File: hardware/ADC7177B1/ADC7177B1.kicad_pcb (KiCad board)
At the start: 4 copper layers, 160 x 100 mm, 185 parts, among them J1 20021111-00010T4LF, J2 RJ45_Wuerth_7499010121A, J3 1715721, J4 Conn_01x01, J5 Conn_01x01, J6 Conn_01x01, J7 Conn_01x01, K1 G6SK-2F-DC5, Q1 SI5618A, Q2 MMBT3904, Q3 FZT851, Q4 FZT951, Q5 FZT851, Q6 MMBT3904, Q7 MMBT3904, U1 STM32H743VITx, U10 TPS7A4901DGN, U11 ADC7177M1, U12 AD8599ARZ, U13 AD8599ARZ, U14 CPC1002N, U15 CPC1002N, U2 24LC08B-E/MS, U3 LAN8742A, U4 THN 15-2425, U5 TEC 3-2419WI, U6 TPS7A4901DGN, U7 TPS7A3001DGN, U8 TPS7A4901DGN, U9 TPS7A4901DGN, Y1 NX5032GA-16, Y2 NX5032GA-25

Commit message: PCB
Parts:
- added H5: MountingHole, MountingHole:MountingHole_2.5mm_Pad_TopBottom, F.Cu at (147.4, 91.4)
- added H6: MountingHole, MountingHole:MountingHole_2.5mm_Pad_TopBottom, F.Cu at (195.4, 91.4)
- added H7: MountingHole, MountingHole:MountingHole_2.5mm_Pad_TopBottom, F.Cu at (147.4, 114.4)
- added H8: MountingHole, MountingHole:MountingHole_2.5mm_Pad_TopBottom, F.Cu at (195.4, 114.4)
- R13, R14: moved to B.Cu
- moved R14 7.73 mm to (237.6, 111.8), turned to -90 degrees
- moved Q2 6.75 mm to (236.0, 105.7)
- moved D3 6.75 mm to (236.0, 108.8)
- moved C30 6.62 mm to (219.8, 96.2)
- moved C33 6.42 mm to (216.3, 96.3)
- moved R12 6.35 mm to (232.0, 100.6), turned to -90 degrees
- moved Q1 6.10 mm to (235.1, 100.7), turned to 90 degrees
- moved D2 5.05 mm to (232.0, 105.7), turned to 90 degrees
- moved R13 3.86 mm to (237.9, 102.9), turned to -90 degrees
- moved C16 3.50 mm to (205.9, 124.7), turned to 0 degrees
- moved C19 3.42 mm to (209.3, 124.7), turned to 180 degrees
- moved C31 1.89 mm to (208.4, 71.8), turned to -90 degrees
- moved C32 1.89 mm to (205.9, 74.9), turned to 90 degrees
- moved C11 1.66 mm to (194.9, 131.3), turned to -90 degrees
- moved C29 1.40 mm to (207.1, 86.9), turned to -90 degrees
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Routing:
- net +15V: track 5.00 -> 127.3 mm, vias 1 -> 6
- net -15V: track 5.08 -> 121.3 mm, vias 1 -> 6
- net +5VD: track 5.71 -> 94.6 mm, vias 2 -> 9
- net Net-(D4-A): track 0.00 -> 68.5 mm, vias 0 -> 9
- net +24V: track 0.00 -> 47.7 mm
- net Net-(D5-K): track 0.00 -> 40.6 mm, vias 0 -> 9
- net GND: track 2.12 -> 40.7 mm, vias 0 -> 42
- net VCCQ: track 0.00 -> 22.2 mm, vias 0 -> 2
- net /Schematic/Ethernet/LED2: track 0.00 -> 17.4 mm, vias 0 -> 1
- net +3.3V: track 15.7 -> 32.5 mm, vias 9 -> 16
- net Net-(D4-K): track 0.00 -> 13.9 mm
- net Net-(D5-A): track 0.00 -> 9.85 mm
- net /Schematic/Ethernet/LED1: track 0.00 -> 9.79 mm
- net Net-(D2-A): track 0.00 -> 9.74 mm
- net Net-(U3-XTAL2): track 0.00 -> 8.38 mm
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- added copper zone on F.Cu, net +15V
- added copper zone on B.Cu, net +24V
- added copper zone on In2.Cu, net +24V
- added copper zone on F.Cu, net +3.3V
- added copper zone on In2.Cu, net +3.3V
- added copper zone on F.Cu, net +5VA
- added copper zone on F.Cu, net +5VD
- added copper zone on In2.Cu, net +5VD
- added copper zone on F.Cu, net -15V
- added copper zone on B.Cu, net GND
- added copper zone on F.Cu, net GND
- added copper zone on In1.Cu, net GND
- added copper zone on B.Cu, net GNDS
- added copper zone on F.Cu, net GNDS
- added copper zone on In1.Cu, net GNDS
- added copper zone on F.Cu, net Net-(D4-A)
- added copper zone on In2.Cu, net Net-(D4-A)
- added copper zone on F.Cu, net Net-(D4-K)
- added copper zone on F.Cu, net Net-(D5-A)
- added copper zone on F.Cu, net Net-(D5-K)
- added copper zone on In2.Cu, net Net-(D5-K)
- added copper zone on F.Cu, net Net-(D6-A)
- added copper zone on In2.Cu, net Net-(D6-A)
- added copper zone on F.Cu, net Net-(D6-K)
- added copper zone on B.Cu, net Net-(J3-Pin_1)
- added copper zone on F.Cu, net Net-(Q3-B)
- added copper zone on F.Cu, net Net-(Q4-B)
- added copper zone on F.Cu, net Net-(Q5-B)
- added copper zone on F.Cu, net Net-(U4-+Vout)
- added copper zone on F.Cu, net Net-(U4--Vout)
- added copper zone on F.Cu, net Net-(U5-+Vout)

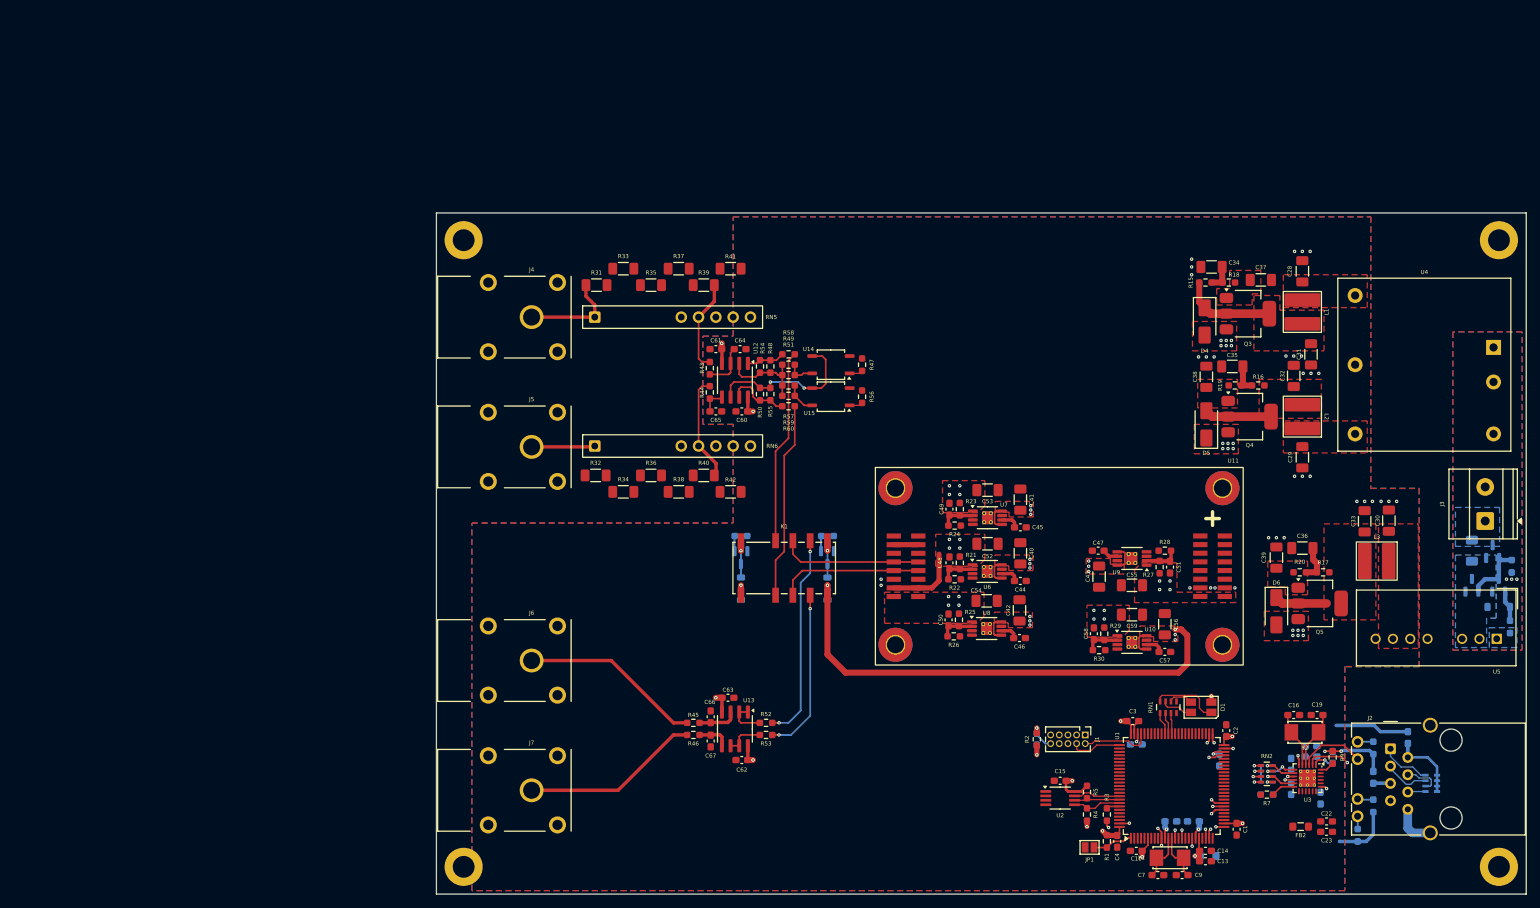
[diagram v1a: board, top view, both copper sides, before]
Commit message: Schematic changes
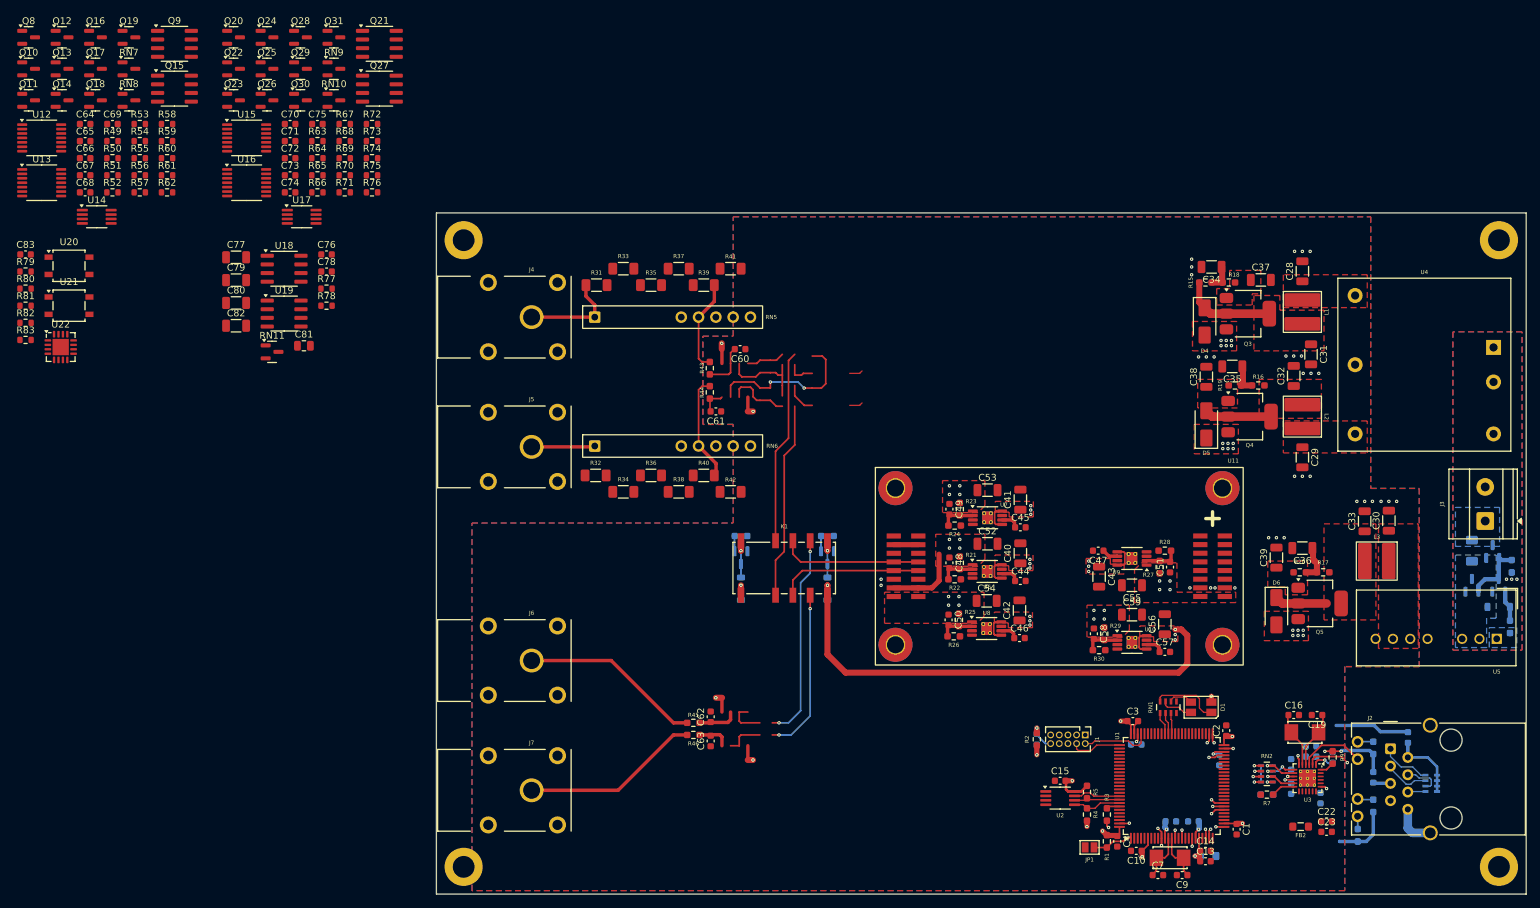
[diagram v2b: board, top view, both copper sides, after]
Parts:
- removed the C60 at (124.8, 80.1)
- removed the C61 at (121.0, 71.0)
- removed the C62 at (124.8, 131.3)
- removed the C63 at (122.8, 122.2)
- removed the R47 at (142.5, 73.3)
- removed the R48 at (129.0, 73.5)
- added C64: 0.1u, Capacitor_SMD:C_0603_1608Metric, F.Cu at (28.4, 37.9)
- added C65: 0.1u, Capacitor_SMD:C_0603_1608Metric, F.Cu at (28.4, 40.5)
- added C66: 0.1u, Capacitor_SMD:C_0603_1608Metric, F.Cu at (28.4, 43.0)
- added C67: 0.1u, Capacitor_SMD:C_0603_1608Metric, F.Cu at (28.4, 45.5)
- added C68: 0.1u, Capacitor_SMD:C_0603_1608Metric, F.Cu at (28.4, 48.0)
- added C69: 0.1u, Capacitor_SMD:C_0603_1608Metric, F.Cu at (32.4, 37.9)
- added C70: 0.1u, Capacitor_SMD:C_0603_1608Metric, F.Cu at (58.5, 37.9)
- added C71: 0.1u, Capacitor_SMD:C_0603_1608Metric, F.Cu at (58.5, 40.5)
- added C72: 0.1u, Capacitor_SMD:C_0603_1608Metric, F.Cu at (58.5, 43.0)
- added C73: 0.1u, Capacitor_SMD:C_0603_1608Metric, F.Cu at (58.5, 45.5)
- added C74: 0.1u, Capacitor_SMD:C_0603_1608Metric, F.Cu at (58.5, 48.0)
- added C75: 0.1u, Capacitor_SMD:C_0603_1608Metric, F.Cu at (62.5, 37.9)
- added C76: 0.1u, Capacitor_SMD:C_0603_1608Metric, F.Cu at (63.9, 57.1)
- added C77: 10u, Capacitor_SMD:C_1206_3216Metric, F.Cu at (50.6, 57.5)
- added C78: 0.1u, Capacitor_SMD:C_0603_1608Metric, F.Cu at (63.9, 59.6)
- added C79: 10u, Capacitor_SMD:C_1206_3216Metric, F.Cu at (50.6, 60.9)
- added C80: 10u, Capacitor_SMD:C_1206_3216Metric, F.Cu at (50.6, 64.2)
- added C81: 2u2, Capacitor_SMD:C_0805_2012Metric, F.Cu at (60.5, 70.5)
- added C82: 10u, Capacitor_SMD:C_1206_3216Metric, F.Cu at (50.6, 67.6)
- added C83: 100p, Capacitor_SMD:C_0603_1608Metric, F.Cu at (19.7, 57.1)
- added Q10: MMBT6429, Package_TO_SOT_SMD:SOT-23, F.Cu at (20.1, 29.8)
- added Q11: MMBF4392, Package_TO_SOT_SMD:SOT-23, F.Cu at (20.1, 34.5)
- added Q12: MMBT6429, Package_TO_SOT_SMD:SOT-23, F.Cu at (25.0, 25.2)
- added Q13: MMBT6429, Package_TO_SOT_SMD:SOT-23, F.Cu at (25.0, 29.8)
- added Q14: MMBT6429, Package_TO_SOT_SMD:SOT-23, F.Cu at (25.0, 34.5)
- added Q15: JFE2140D, Package_SO:SOIC-8_3.9x4.9mm_P1.27mm, F.Cu at (41.5, 32.8)
- added Q16: MMBT6429, Package_TO_SOT_SMD:SOT-23, F.Cu at (29.9, 25.2)
- added Q17: MMBF4392, Package_TO_SOT_SMD:SOT-23, F.Cu at (29.9, 29.8)
- added Q18: MMBT6429, Package_TO_SOT_SMD:SOT-23, F.Cu at (29.9, 34.5)
- added Q19: MMBT6429, Package_TO_SOT_SMD:SOT-23, F.Cu at (34.9, 25.2)
- added Q20: MMBT6429, Package_TO_SOT_SMD:SOT-23, F.Cu at (50.2, 25.2)
- added Q21: JFE2140D, Package_SO:SOIC-8_3.9x4.9mm_P1.27mm, F.Cu at (71.6, 26.2)
- added Q22: MMBT6429, Package_TO_SOT_SMD:SOT-23, F.Cu at (50.2, 29.8)
- added Q23: MMBF4392, Package_TO_SOT_SMD:SOT-23, F.Cu at (50.2, 34.5)
- added Q24: MMBT6429, Package_TO_SOT_SMD:SOT-23, F.Cu at (55.1, 25.2)
- added Q25: MMBT6429, Package_TO_SOT_SMD:SOT-23, F.Cu at (55.1, 29.8)
- added Q26: MMBT6429, Package_TO_SOT_SMD:SOT-23, F.Cu at (55.1, 34.5)
- added Q27: JFE2140D, Package_SO:SOIC-8_3.9x4.9mm_P1.27mm, F.Cu at (71.6, 32.8)
- added Q28: MMBT6429, Package_TO_SOT_SMD:SOT-23, F.Cu at (60.0, 25.2)
- added Q29: MMBF4392, Package_TO_SOT_SMD:SOT-23, F.Cu at (60.0, 29.8)
- added Q30: MMBT6429, Package_TO_SOT_SMD:SOT-23, F.Cu at (60.0, 34.5)
- added Q31: MMBT6429, Package_TO_SOT_SMD:SOT-23, F.Cu at (65.0, 25.2)
- added Q8: MMBT6429, Package_TO_SOT_SMD:SOT-23, F.Cu at (20.1, 25.2)
- added Q9: JFE2140D, Package_SO:SOIC-8_3.9x4.9mm_P1.27mm, F.Cu at (41.5, 26.2)
- added R61: 2k/0.1%, Resistor_SMD:R_0603_1608Metric, F.Cu at (40.5, 45.5)
- added R62: 21k5/0.125W, Resistor_SMD:R_0603_1608Metric, F.Cu at (40.5, 48.0)
- added R63: 14k7, Resistor_SMD:R_0603_1608Metric, F.Cu at (62.5, 40.5)
- added R64: 21k5/0.125W, Resistor_SMD:R_0603_1608Metric, F.Cu at (62.5, 43.0)
- added R65: 21k5/0.125W, Resistor_SMD:R_0603_1608Metric, F.Cu at (62.5, 45.5)
- added R66: 2k/0.1%, Resistor_SMD:R_0603_1608Metric, F.Cu at (62.5, 48.0)
- added R67: 2k/0.1%, Resistor_SMD:R_0603_1608Metric, F.Cu at (66.5, 37.9)
- added R68: 2k/0.1%, Resistor_SMD:R_0603_1608Metric, F.Cu at (66.5, 40.5)
- added R69: 21k5/0.125W, Resistor_SMD:R_0603_1608Metric, F.Cu at (66.5, 43.0)
- added R70: 14k7, Resistor_SMD:R_0603_1608Metric, F.Cu at (66.5, 45.5)
- added R71: 21k5/0.125W, Resistor_SMD:R_0603_1608Metric, F.Cu at (66.5, 48.0)
- added R72: 21k5/0.125W, Resistor_SMD:R_0603_1608Metric, F.Cu at (70.5, 37.9)
- added R73: 2k/0.1%, Resistor_SMD:R_0603_1608Metric, F.Cu at (70.5, 40.5)
- added R74: 2k/0.1%, Resistor_SMD:R_0603_1608Metric, F.Cu at (70.5, 43.0)
- added R75: 2k/0.1%, Resistor_SMD:R_0603_1608Metric, F.Cu at (70.5, 45.5)
- added R76: 21k5/0.125W, Resistor_SMD:R_0603_1608Metric, F.Cu at (70.5, 48.0)
- added R77: 10k/0.01%/2ppm, Resistor_SMD:R_0603_1608Metric, F.Cu at (63.9, 62.1)
- added R78: 10k/0.01%/2ppm, Resistor_SMD:R_0603_1608Metric, F.Cu at (63.9, 64.6)
- added R79: 1k, Resistor_SMD:R_0603_1608Metric, F.Cu at (19.7, 59.6)
- added R80: 1k, Resistor_SMD:R_0603_1608Metric, F.Cu at (19.7, 62.1)
- added R81: 5k49/0.1%/10ppm, Resistor_SMD:R_0603_1608Metric, F.Cu at (19.7, 64.6)
- added R82: 499/0.01%/2ppm, Resistor_SMD:R_0603_1608Metric, F.Cu at (19.7, 67.1)
- added R83: 10k, Resistor_SMD:R_0603_1608Metric, F.Cu at (19.7, 69.6)
- added RN10: MPMT4001AT1, Package_TO_SOT_SMD:SOT-23, F.Cu at (65.0, 34.5)
- added RN11: MPMT2002AT5, Package_TO_SOT_SMD:SOT-23, F.Cu at (55.9, 71.4)
- added RN7: MPMT4001AT1, Package_TO_SOT_SMD:SOT-23, F.Cu at (34.9, 29.8)
- added RN8: MPMT4001AT1, Package_TO_SOT_SMD:SOT-23, F.Cu at (34.9, 34.5)
- added RN9: MPMT4001AT1, Package_TO_SOT_SMD:SOT-23, F.Cu at (65.0, 29.8)
- added U16: ADA4077-4ARUZ, Package_SO:TSSOP-14_4.4x5mm_P0.65mm, F.Cu at (52.1, 46.6)
- added U17: ADA4077-2ARMZ, Package_SO:MSOP-8_3x3mm_P0.65mm, F.Cu at (60.2, 51.6)
- added U18: AD8676xR, Package_SO:SOIC-8_3.9x4.9mm_P1.27mm, F.Cu at (57.6, 59.2)
- added U19: MAX6350ESA, Package_SO:SOIC-8_3.9x4.9mm_P1.27mm, F.Cu at (57.6, 65.8)
- added U20: AQY212G3HS, Package_SO:SO-4_4.4x4.3mm_P2.54mm, F.Cu at (26.1, 58.8)
- added U21: AQY212G3HS, Package_SO:SO-4_4.4x4.3mm_P2.54mm, F.Cu at (26.1, 64.6)
- added U22: AD8222xCPZ, Package_CSP:LFCSP-16-1EP_4x4mm_P0.65mm_EP2.4x2.4mm, F.Cu at (24.8, 70.7)
- C1, C10, C11, C12, C13, C14, C15, C16, C17, C18, C19, C2, C20, C21, C22, C23, C24, C25, C26, C27, C3, C4, C44, C45, C46, C47, C48, C49, C5, C50, C51, C57, C58, C6, C7, C8, C9: footprint Capacitor_SMD:C_0603_1608Metric_Pad1.08x0.95mm_HandSolder -> Capacitor_SMD:C_0603_1608Metric
- C28, C29, C30, C31, C32, C33, C34, C35, C36, C37, C38, C39, C40, C41, C42, C43, C52, C53, C54, C55, C56, C59: footprint Capacitor_SMD:C_1206_3216Metric_Pad1.33x1.80mm_HandSolder -> Capacitor_SMD:C_1206_3216Metric
- C60: renamed from C64; footprint Capacitor_SMD:C_0603_1608Metric_Pad1.08x0.95mm_HandSolder -> Capacitor_SMD:C_0603_1608Metric
- C61: renamed from C65; footprint Capacitor_SMD:C_0603_1608Metric_Pad1.08x0.95mm_HandSolder -> Capacitor_SMD:C_0603_1608Metric
- C62: renamed from C66; footprint Capacitor_SMD:C_0603_1608Metric_Pad1.08x0.95mm_HandSolder -> Capacitor_SMD:C_0603_1608Metric
- C63: renamed from C67; footprint Capacitor_SMD:C_0603_1608Metric_Pad1.08x0.95mm_HandSolder -> Capacitor_SMD:C_0603_1608Metric
- R49: value DNP -> 14k7; footprint Resistor_SMD:R_0603_1608Metric_Pad0.98x0.95mm_HandSolder -> Resistor_SMD:R_0603_1608Metric
- R50, R55: value 10k/0.1% -> 21k5/0.125W; footprint Resistor_SMD:R_0603_1608Metric_Pad0.98x0.95mm_HandSolder -> Resistor_SMD:R_0603_1608Metric
- R51: value 1k1/0.1% -> 21k5/0.125W; footprint Resistor_SMD:R_0603_1608Metric_Pad0.98x0.95mm_HandSolder -> Resistor_SMD:R_0603_1608Metric
- R52, R53, R60: value 510 -> 2k/0.1%; footprint Resistor_SMD:R_0603_1608Metric_Pad0.98x0.95mm_HandSolder -> Resistor_SMD:R_0603_1608Metric
- R54: value 10k/0.1% -> 2k/0.1%; footprint Resistor_SMD:R_0603_1608Metric_Pad0.98x0.95mm_HandSolder -> Resistor_SMD:R_0603_1608Metric
- R56: value 1k2 -> 14k7; footprint Resistor_SMD:R_0603_1608Metric_Pad0.98x0.95mm_HandSolder -> Resistor_SMD:R_0603_1608Metric
- R57: value 1k2 -> 21k5/0.125W; footprint Resistor_SMD:R_0603_1608Metric_Pad0.98x0.95mm_HandSolder -> Resistor_SMD:R_0603_1608Metric
- R58: value 510 -> 21k5/0.125W; footprint Resistor_SMD:R_0603_1608Metric_Pad0.98x0.95mm_HandSolder -> Resistor_SMD:R_0603_1608Metric
- R59: value 110/0.05% -> 2k/0.1%; footprint Resistor_SMD:R_0603_1608Metric_Pad0.98x0.95mm_HandSolder -> Resistor_SMD:R_0603_1608Metric
- U12, U13: value AD8599ARZ -> ADA4077-4ARUZ; footprint Package_SO:SOIC-8_3.9x4.9mm_P1.27mm -> Package_SO:TSSOP-14_4.4x5mm_P0.65mm
- U14: value CPC1002N -> ADA4077-2ARMZ; footprint Package_SO:SOP-4_3.8x4.1mm_P2.54mm -> Package_SO:MSOP-8_3x3mm_P0.65mm
- U15: value CPC1002N -> ADA4077-4ARUZ; footprint Package_SO:SOP-4_3.8x4.1mm_P2.54mm -> Package_SO:TSSOP-14_4.4x5mm_P0.65mm
- moved U13 129.6 mm to (22.1, 46.6), turned to 0 degrees
- moved R53 128.5 mm to (36.5, 37.9)
- moved R52 123.6 mm to (32.4, 48.0)
- moved R56 110.9 mm to (36.5, 45.5), turned to 0 degrees
- moved U14 110.0 mm to (30.1, 51.6), turned to 0 degrees
- moved U12 107.8 mm to (22.1, 40.0), turned to 0 degrees
- moved R49 104.5 mm to (32.4, 40.5)
- moved R51 103.5 mm to (32.4, 45.5)
- moved R50 101.2 mm to (32.4, 43.0), turned to 0 degrees
- moved R57 99.4 mm to (36.5, 48.0)
- moved R55 98.8 mm to (36.5, 43.0), turned to 0 degrees
- moved R59 98.6 mm to (40.5, 40.5)
- moved R60 98.2 mm to (40.5, 43.0)
- moved R58 97.3 mm to (40.5, 37.9)
- moved R54 96.9 mm to (36.5, 40.5), turned to 0 degrees
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- renumbered R61 to R47, R62 to R48
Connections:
- C60 pad 2: Net-(U12A-+) -> /Schematic/Frontend/Analog Channels A/INA_P
- C61 pad 2: Net-(U12B-+) -> /Schematic/Frontend/Analog Channels A/INA_N
- C62 pad 1: Net-(U13A-+) -> GND
- C62 pad 2: GND -> /Schematic/Frontend/Analog Channels B/INB_P
- C63 pad 2: Net-(U13B-+) -> /Schematic/Frontend/Analog Channels B/INB_N
- K1 pad 10: Net-(K1-Pad10) -> /Schematic/Frontend/Gain/OUT_P
- K1 pad 3: Net-(K1-Pad3) -> /Schematic/Frontend/Gain/OUT_N
- K1 pad 5: Net-(K1-Pad5) -> /Schematic/Frontend/Analog Channels B/OUTB_N
- K1 pad 8: Net-(K1-Pad8) -> /Schematic/Frontend/Analog Channels B/OUTB_P
- R43 pad 2: Net-(U12A-+) -> /Schematic/Frontend/Analog Channels A/INA_P
- R44 pad 2: Net-(U12B-+) -> /Schematic/Frontend/Analog Channels A/INA_N
- R45 pad 2: Net-(U13A-+) -> /Schematic/Frontend/Analog Channels B/INB_P
- R46 pad 2: Net-(U13B-+) -> /Schematic/Frontend/Analog Channels B/INB_N
- R49 pad 1: Net-(U12A--) -> +10V
- R49 pad 2: Net-(R49-Pad2) -> Net-(U14A--)
- R50 pad 1: Net-(U12B--) -> Net-(Q10-E)
- R50 pad 2: Net-(R50-Pad2) -> Net-(Q10-B)
- R51 pad 1: Net-(U12A--) -> Net-(U14A--)
- R51 pad 2: Net-(R49-Pad2) -> Net-(U12A-+)
- R52 pad 1: Net-(U13A--) -> Net-(Q10-E)
- R52 pad 2: Net-(K1-Pad8) -> Net-(R52-Pad2)
- R53 pad 1: Net-(U13B--) -> Net-(U12A-+)
- R53 pad 2: Net-(K1-Pad5) -> Net-(R52-Pad2)
- R54 pad 1: Net-(U12A--) -> Net-(R52-Pad2)
- R54 pad 2: Net-(R48-Pad2) -> Net-(Q12-E)
- R55 pad 1: Net-(U12B--) -> Net-(Q12-E)
- R55 pad 2: Net-(R50-Pad2) -> Net-(Q12-B)
- R56 pad 1: /Schematic/Frontend/Gx100 -> +10V
- R56 pad 2: Net-(R56-Pad2) -> Net-(U14B--)
- R57 pad 1: Net-(U12A--) -> Net-(Q16-E)
- R57 pad 2: Net-(R57-Pad2) -> Net-(Q14-E)
- R58 pad 1: Net-(R48-Pad2) -> Net-(U14B--)
- R58 pad 2: Net-(K1-Pad10) -> Net-(U13A-+)
- R59 pad 1: Net-(U12A--) -> Net-(Q16-E)
- R59 pad 2: Net-(R57-Pad2) -> Net-(R59-Pad2)
- R60 pad 1: Net-(R50-Pad2) -> Net-(U13A-+)
- R60 pad 2: Net-(K1-Pad3) -> Net-(R59-Pad2)
- U12 pad 1: Net-(R48-Pad2) -> Net-(Q8-B)
- U12 pad 2: Net-(U12A--) -> Net-(Q10-E)
- U12 pad 4: -15V -> +15V
- U12 pad 5: Net-(U12B-+) -> Net-(U12A-+)
- U12 pad 6: Net-(U12B--) -> Net-(Q12-E)
- U12 pad 7: Net-(R50-Pad2) -> Net-(Q13-B)
- U12 pad 8: +15V -> /Schematic/Frontend/Analog Channels A/OUTA_P
- U13 pad 1: Net-(U13A--) -> Net-(Q14-B)
- U13 pad 2: Net-(U13A--) -> Net-(Q16-E)
- U13 pad 4: -15V -> +15V
- U13 pad 5: Net-(U13B-+) -> Net-(U13A-+)
- U13 pad 6: Net-(U13B--) -> Net-(Q18-E)
- U13 pad 7: Net-(U13B--) -> Net-(Q19-B)
- U13 pad 8: +15V -> /Schematic/Frontend/Analog Channels A/OUTA_N
- U14 pad 1: Net-(R47-Pad2) -> Net-(R52-Pad2)
- U14 pad 2: GND -> Net-(U14A--)
- U14 pad 3: Net-(U12B--) -> GND
- U14 pad 4: Net-(R49-Pad2) -> -15V
- U15 pad 1: Net-(R56-Pad2) -> Net-(Q20-B)
- U15 pad 2: GND -> Net-(Q22-E)
- U15 pad 3: Net-(U12B--) -> Net-(U15A-+)
- U15 pad 4: Net-(R57-Pad2) -> +15V
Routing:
- net (no net): track 0.00 -> 75.8 mm, vias 0 -> 2
- net Net-(K1-Pad8): track 30.4 -> 0.00 mm, vias 2 -> 0
- net /Schematic/Frontend/Analog Channels B/OUTB_P: track 0.00 -> 30.4 mm, vias 0 -> 2
- net Net-(K1-Pad3): track 28.9 -> 0.00 mm
- net /Schematic/Frontend/Gain/OUT_N: track 0.00 -> 28.9 mm
- net Net-(K1-Pad10): track 28.5 -> 0.00 mm
- net /Schematic/Frontend/Gain/OUT_P: track 0.00 -> 28.5 mm
- net Net-(K1-Pad5): track 24.4 -> 0.00 mm, vias 2 -> 0
- net /Schematic/Frontend/Analog Channels B/OUTB_N: track 0.00 -> 24.4 mm, vias 0 -> 2
- net Net-(U12B--): track 23.5 -> 0.00 mm, vias 2 -> 0
- net Net-(U12A--): track 13.0 -> 0.00 mm
- net Net-(R50-Pad2): track 9.39 -> 0.00 mm
- net Net-(U12A-+): track 6.81 -> 0.00 mm
- net /Schematic/Frontend/Analog Channels A/INA_P: track 0.00 -> 6.81 mm
- net Net-(U13A--): track 5.73 -> 0.00 mm
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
